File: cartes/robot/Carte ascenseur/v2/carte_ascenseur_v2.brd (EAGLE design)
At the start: 55.9 x 66 mm, 41 parts, among them IC2 7805TV, U1 MCP2551, U2 ADUM1250ARZ, U3 ADUM1400ARWZ, X1 12V Dirty, X2 5V Dirty

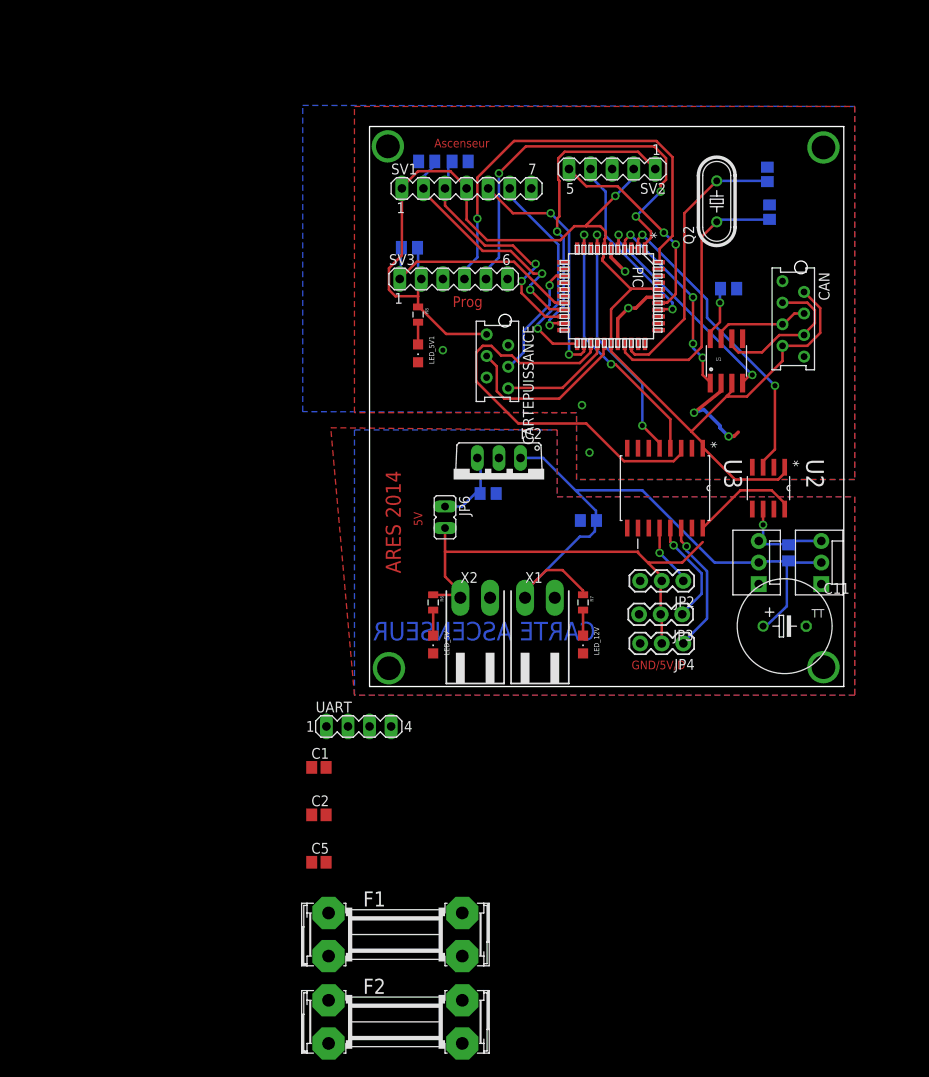
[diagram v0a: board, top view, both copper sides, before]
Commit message: Maj carte ascenseur
Fusible, condo d'alim, jumper triple pour l'alim 5V, LED pour le PIC,
sortie UART
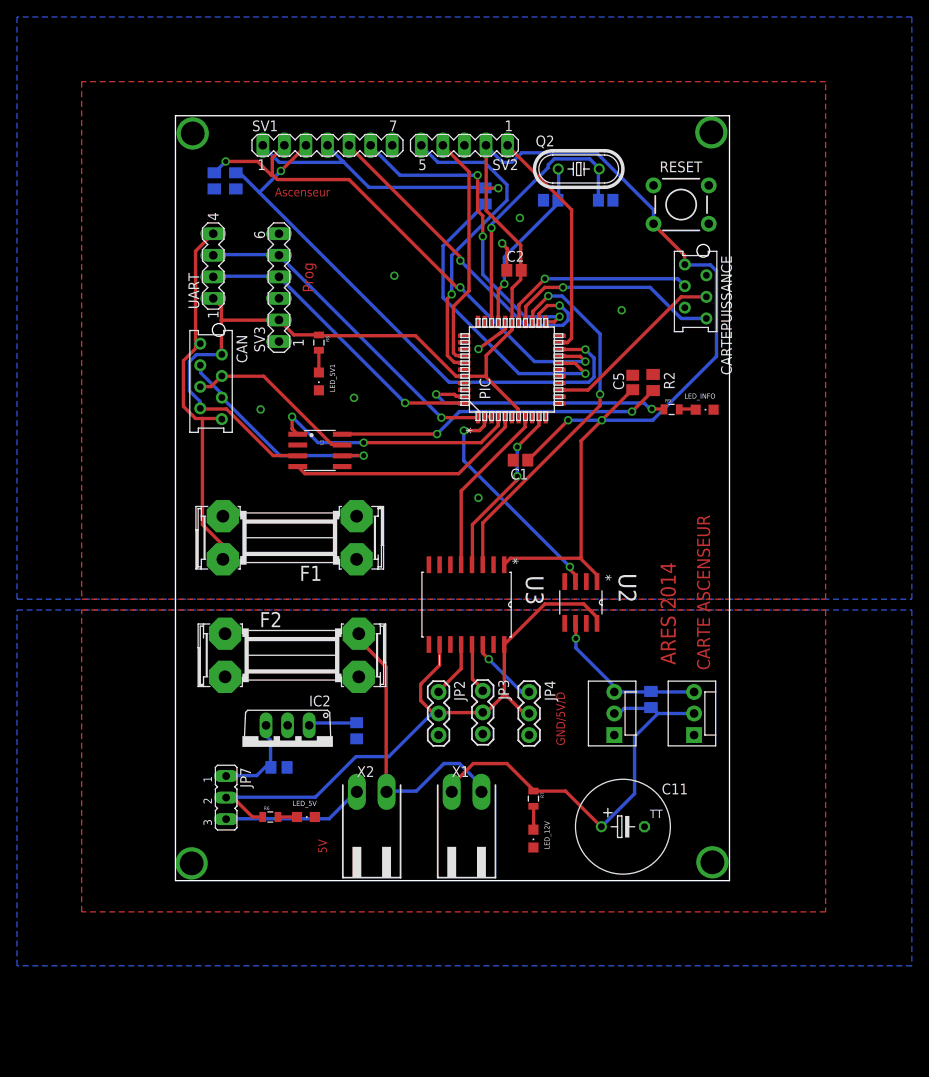
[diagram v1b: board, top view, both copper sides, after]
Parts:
- removed JP6: (no value), jumper:JP1
- added JP7: (no value), jumper:JP2
- added LED_INFO: (no value), adafruit:CHIPLED_0805
- added R9: 200, SparkFun-Passives:0805
- added RESET: SWITCH-MOMENTARY-2PTH, SparkFun-Electromechanical:TACTILE-PTH
- R6, R8: value 1k -> 200
- moved CAN 69.0 mm to (2.54, 39.0)
- moved C2 68.1 mm to (38.2, 47.6)
- moved C5 67.5 mm to (52.2, 34.4), turned to 90 degrees
- moved UART 56.9 mm to (2.79, 48.1), turned to 90 degrees
- moved U1 49.0 mm to (15.4, 26.4), turned to 270 degrees
- moved F1 48.4 mm to (11.8, 16.1), turned to 180 degrees
- moved F2 44.9 mm to (12.1, 2.29)
- moved C1 43.3 mm to (39.0, 25.3), turned to 180 degrees
- moved C9 40.6 mm to (10.5, -10.9)
- moved IC2 40.1 mm to (11.6, -8.51)
- moved C10 36.9 mm to (19.7, -6.60), turned to 90 degrees
- moved R6 31.7 mm to (9.53, -16.8), turned to 0 degrees
- moved JP2 31.7 mm to (29.3, -2.03), turned to 270 degrees
- moved C11 30.3 mm to (51.1, -17.9)
- moved U3 27.1 mm to (32.6, 8.26)
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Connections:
- removed net 5V_FUSE: F2.1A, U2.8, U3.10, U3.16
- removed net UART_RX: PIC.35, UART.3
- removed net UART_TX: PIC.32, UART.2
- removed net VCC_FUSE: F1.1A, U2.1, U3.1
- new net N$25: PIC.43, R9.1
- new net N$27: F2.2A, X1.2, X2.2
- new net N$29: CAN.1, CAN.8, F1.2A, UART.4
- new net N$30: PIC.18, R3.1
- new net N$31: JP7.3, X2.1
- new net N$32: C10.2, IC2.1
- new net N$5: LED_INFO.A, R9.2
- net !MCLR!: no longer PIC.18, R3.1
- net +12V: no longer C10.2, IC2.1
- net +5V: now also JP7.2, U2.8, U3.10, U3.16; no longer F2.2A, JP6.2, X2.1
- net GND1: now also F1.1A, LED_INFO.C, RESET.1; no longer CAN.1, CAN.8, UART.4
- net GND2: now also F2.1A; no longer X1.2, X2.2
- net N$6: now also JP7.1; no longer JP6.1
- net PGC: now also UART.3
- net PGD: now also UART.2
- net VCC: now also RESET.3, U2.1, U3.1; no longer F1.2A
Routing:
- net VCC: track 137.3 -> 244.5 mm, vias 1 -> 3
- net N$29: track 0.00 -> 45.9 mm
- net N$30: track 0.00 -> 37.1 mm, vias 0 -> 1
- net FCB: track 30.3 -> 67.3 mm
- net N$27: track 0.00 -> 34.4 mm
- net N$4: track 6.43 -> 38.8 mm, vias 1 -> 2
- net FCH: track 29.5 -> 61.5 mm, vias 2 -> 3
- net N$25: track 0.00 -> 31.0 mm, vias 0 -> 2
- net +12V: track 78.1 -> 48.8 mm
- net !MCLR!: track 25.9 -> 0.00 mm
- net +5V: track 54.8 -> 77.4 mm
- net N$31: track 0.00 -> 16.8 mm
- net GND1: track 24.2 -> 8.30 mm, vias 7 -> 8
- net PGD: track 51.2 -> 35.8 mm
- net QEB: track 25.3 -> 39.0 mm, vias 1 -> 3
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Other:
- board size 55.9 x 66 mm -> 65.3 x 90.1 mm

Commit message: Maj carte ascenseur
2 via moins
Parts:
- flipped R1 to the top
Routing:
- net N$27: track 34.4 -> 78.0 mm
- net +5V: track 77.4 -> 86.1 mm
- net +12V: track 48.8 -> 56.7 mm
- net N$8: track 8.37 -> 9.32 mm, vias 1 -> 0
- net FCH: track 61.5 -> 61.9 mm, vias 3 -> 2
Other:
- board size 65.3 x 90.1 mm -> 67.8 x 90.1 mm
- board text added: "Couleur"
- board text added: "Reset"
- board text added: "VCC/TX/RX/GND"

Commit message: change isolate, airwaves qui en découlaient de ce changement, épaisseur sérigraphie et sérigraphie de certains composants
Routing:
- net GND1: track 8.30 -> 39.1 mm, vias 8 -> 9
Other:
- board text added: "12V"
- board text added: "7805"
- board text added: "GND"
- board text added: "Weidmuller"
- board text added: "v2"
